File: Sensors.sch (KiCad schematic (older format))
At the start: 0 parts

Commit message: Schematic v0.2
Added IC and wiring
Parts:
- added P11, P13: CONN_01X07, symbol CONN_01X07
- added P12, P14: CONN_01X04, symbol CONN_01X04
- added P15: DHT22, symbol CONN_01X03
- added P16: GY-87, symbol CONN_01X08
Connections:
- new net +BATT: P11.2 (P2), P13.1 (P1), P15.2 (P2), P16.1 (P1)
- new net A0: P12.4 (P4)
- new net A1: P12.3 (P3)
- new net A2: P12.2 (P2)
- new net A3: P12.1 (P1)
- new net D7: P14.3 (P3)
- new net D8: P14.4 (P4)
- new net DHT/D6: P11.7 (P7), P15.1 (P1)
- new net DRDY: P16.8 (P8)
- new net FSYNC: P16.6 (P6)
- new net GND: P11.1 (P1), P13.2 (P2), P15.3 (P3), P16.2 (P2)
- new net INT0: P14.1 (P1)
- new net INT1: P14.2 (P2)
- new net INTA: P16.7 (P7)
- new net MISO: P13.4 (P4)
- new net MOSI: P13.5 (P5)
- new net NSS: P13.6 (P6)
- new net RST: P13.7 (P7)
- new net SCK: P13.3 (P3)
- new net SCL: P11.3 (P3), P16.4 (P4)
- new net SDA: P11.4 (P4), P16.5 (P5)
- new net S_RX: P11.5 (P5)
- new net S_TX: P11.6 (P6)
- no-connect marks 0 -> 4

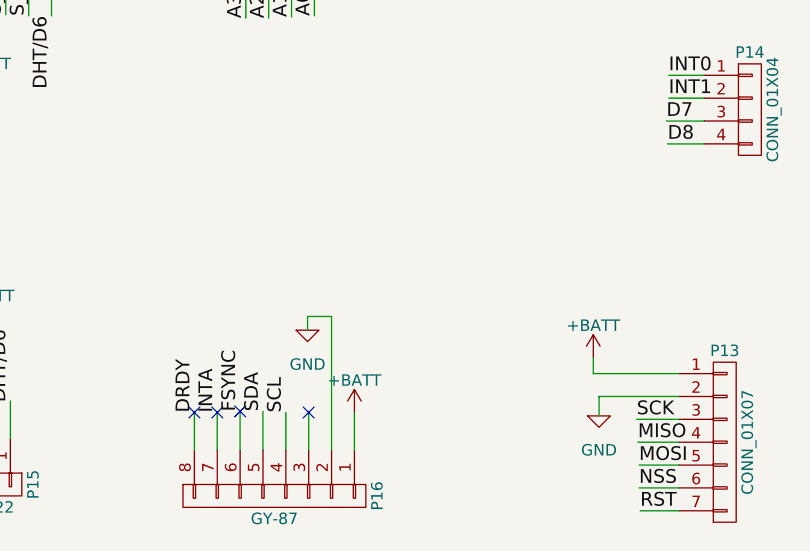
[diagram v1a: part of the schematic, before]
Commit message: Fix arduino mini pro pin 6 bug, added capacitors
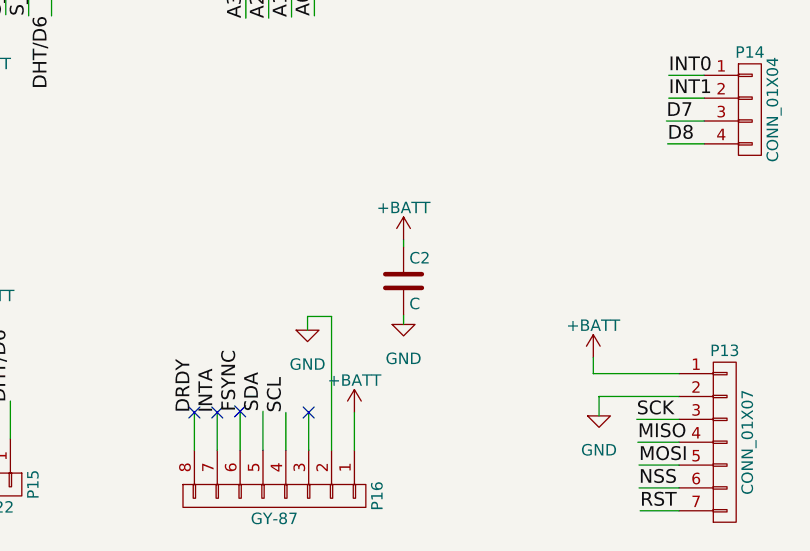
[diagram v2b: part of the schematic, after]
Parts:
- added C2: C, symbol C
- P11, P13: footprint (none) -> Pin_Headers:Pin_Header_Straight_1x07
- P12, P14: footprint (none) -> Pin_Headers:Pin_Header_Straight_1x04
- P15: footprint (none) -> Pin_Headers:Pin_Header_Straight_1x03
- P16: footprint (none) -> Pin_Headers:Pin_Header_Straight_1x08
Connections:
- net +BATT: now also C2.1
- net GND: now also C2.2
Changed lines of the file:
@@
 EESchema Schematic File Version 2
+LIBS:CatSat-rescue
 LIBS:power
 LIBS:device
@@
 LIBS:contrib
 LIBS:valves
-LIBS:ArduProMiniTKB
-LIBS:L80-M39
-LIBS:RFM95W-868S2
-LIBS:theinventorhouse
 LIBS:CatSat-cache
+LIBS:rfm95
 EELAYER 25 0
 EELAYER END
@@
 F 0 "P13" H 7765 5020 50  0000 C CNN
 F 1 "CONN_01X07" V 7865 4620 50  0000 C CNN
-F 2 "" H 7765 4620 50  0000 C CNN
+F 2 "Pin_Headers:Pin_Header_Straight_1x07" H 7765 4620 50  0001 C CNN
 F 3 "" H 7765 4620 50  0000 C CNN
 	1    7765 4620
@@
 F 0 "P14" H 7875 3415 50  0000 C CNN
 F 1 "CONN_01X04" V 7975 3165 50  0000 C CNN
-F 2 "" H 7875 3165 50  0000 C CNN
+F 2 "Pin_Headers:Pin_Header_Straight_1x04" H 7875 3165 50  0001 C CNN
 F 3 "" H 7875 3165 50  0000 C CNN
 	1    7875 3165
@@
 F 0 "P12" H 5820 2625 50  0000 C CNN
 F 1 "CONN_01X04" V 5920 2375 50  0000 C CNN
-F 2 "" H 5820 2375 50  0000 C CNN
+F 2 "Pin_Headers:Pin_Header_Straight_1x04" H 5820 2375 50  0001 C CNN
 F 3 "" H 5820 2375 50  0000 C CNN
 	1    5820 2375
@@
 F 0 "P11" H 4520 2780 50  0000 C CNN
 F 1 "CONN_01X07" V 4620 2380 50  0000 C CNN
-F 2 "" H 4520 2380 50  0000 C CNN
+F 2 "Pin_Headers:Pin_Header_Straight_1x07" H 4520 2380 50  0001 C CNN
 F 3 "" H 4520 2380 50  0000 C CNN
 	1    4520 2380
@@
 $EndComp
 $Comp
-L +BATT #PWR017
+L +BATT #PWR021
 U 1 1 579A5A93
 P 4525 3105
-F 0 "#PWR017" H 4525 2955 50  0001 C CNN
+F 0 "#PWR021" H 4525 2955 50  0001 C CNN
 F 1 "+BATT" H 4525 3245 50  0000 C CNN
 F 2 "" H 4525 3105 50  0000 C CNN
@@
 A0
 $Comp
-L GND #PWR018
+L GND #PWR022
 U 1 1 579A5AA2
 P 4220 2650
-F 0 "#PWR018" H 4220 2400 50  0001 C CNN
+F 0 "#PWR022" H 4220 2400 50  0001 C CNN
 F 1 "GND" H 4220 2500 50  0000 C CNN
 F 2 "" H 4220 2650 50  0000 C CNN
@@
 A3
 $Comp
-L GND #PWR019
+L GND #PWR023
 U 1 1 579A7C37
 P 7215 4505
-F 0 "#PWR019" H 7215 4255 50  0001 C CNN
+F 0 "#PWR023" H 7215 4255 50  0001 C CNN
 F 1 "GND" H 7215 4355 50  0000 C CNN
 F 2 "" H 7215 4505 50  0000 C CNN
@@
 $EndComp
 $Comp
-L +BATT #PWR020
+L +BATT #PWR024
 U 1 1 579A7C57
 P 7190 4250
-F 0 "#PWR020" H 7190 4100 50  0001 C CNN
+F 0 "#PWR024" H 7190 4100 50  0001 C CNN
 F 1 "+BATT" H 7190 4390 50  0000 C CNN
 F 2 "" H 7190 4250 50  0000 C CNN
@@
 F 0 "P15" H 4540 5005 50  0000 C CNN
 F 1 "DHT22" V 4640 4805 50  0000 C CNN
-F 2 "" H 4540 4805 50  0000 C CNN
+F 2 "Pin_Headers:Pin_Header_Straight_1x03" H 4540 4805 50  0001 C CNN
 F 3 "" H 4540 4805 50  0000 C CNN
 	1    4540 4805
@@
 F 0 "P16" H 5795 5305 50  0000 C CNN
 F 1 "GY-87" V 5895 4855 50  0000 C CNN
-F 2 "" H 5795 4855 50  0000 C CNN
+F 2 "Pin_Headers:Pin_Header_Straight_1x08" H 5795 4855 50  0001 C CNN
 F 3 "" H 5795 4855 50  0000 C CNN
 	1    5795 4855
@@
 SCL
 $Comp
-L +BATT #PWR021
+L +BATT #PWR025
 U 1 1 579A9426
 P 6145 4490
-F 0 "#PWR021" H 6145 4340 50  0001 C CNN
+F 0 "#PWR025" H 6145 4340 50  0001 C CNN
 F 1 "+BATT" H 6145 4630 50  0000 C CNN
 F 2 "" H 6145 4490 50  0000 C CNN
@@
 $EndComp
 $Comp
-L GND #PWR022
+L GND #PWR026
 U 1 1 579A9468
 P 5940 4130
-F 0 "#PWR022" H 5940 3880 50  0001 C CNN
+F 0 "#PWR026" H 5940 3880 50  0001 C CNN
 F 1 "GND" H 5940 3980 50  0000 C CNN
 F 2 "" H 5940 4130 50  0000 C CNN
@@
 NoConn ~ 5945 4490
 $Comp
-L GND #PWR023
+L GND #PWR027
 U 1 1 579A95AE
 P 4280 4450
-F 0 "#PWR023" H 4280 4200 50  0001 C CNN
+F 0 "#PWR027" H 4280 4200 50  0001 C CNN
 F 1 "GND" H 4280 4300 50  0000 C CNN
 F 2 "" H 4280 4450 50  0000 C CNN
@@
 $EndComp
 $Comp
-L +BATT #PWR024
+L +BATT #PWR028
 U 1 1 579A95D4
 P 4540 4120
-F 0 "#PWR024" H 4540 3970 50  0001 C CNN
+F 0 "#PWR028" H 4540 3970 50  0001 C CNN
 F 1 "+BATT" H 4540 4260 50  0000 C CNN
 F 2 "" H 4540 4120 50  0000 C CNN
@@
 NoConn ~ 5545 4490
 NoConn ~ 5645 4485
+$Comp
+L GND #PWR?
+U 1 1 579BCD75
+P 6360 4105
+F 0 "#PWR?" H 6360 3855 50  0001 C CNN
+F 1 "GND" H 6360 3955 50  0000 C CNN
+F 2 "" H 6360 4105 50  0000 C CNN
+F 3 "" H 6360 4105 50  0000 C CNN
+	1    6360 4105
+	1    0    0    -1
+$EndComp
+$Comp
+L +BATT #PWR?
+U 1 1 579BCD92
+P 6360 3735
+F 0 "#PWR?" H 6360 3585 50  0001 C CNN
+F 1 "+BATT" H 6360 3875 50  0000 C CNN
+F 2 "" H 6360 3735 50  0000 C CNN
+F 3 "" H 6360 3735 50  0000 C CNN
+	1    6360 3735
+	1    0    0    -1
+$EndComp
+$Comp
+L C C2
+U 1 1 579BCEC3
+P 6360 3915
+F 0 "C2" H 6385 4015 50  0000 L CNN
+F 1 "C" H 6385 3815 50  0000 L CNN
+F 2 "" H 6398 3765 30  0000 C CNN
+F 3 "" H 6360 3915 60  0000 C CNN
+	1    6360 3915
+	1    0    0    -1
+$EndComp
+Wire Wire Line
+	6360 3765 6360 3735
+Wire Wire Line
+	6360 4065 6360 4105
 $EndSCHEMATC

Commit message: Finished telemtry PCB
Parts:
- C2: footprint (none) -> Capacitors_ThroughHole:C_Disc_D6_P5
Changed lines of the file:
@@
 $EndComp
 $Comp
-L +BATT #PWR021
+L +BATT #PWR025
 U 1 1 579A5A93
 P 4525 3105
-F 0 "#PWR021" H 4525 2955 50  0001 C CNN
+F 0 "#PWR025" H 4525 2955 50  0001 C CNN
 F 1 "+BATT" H 4525 3245 50  0000 C CNN
 F 2 "" H 4525 3105 50  0000 C CNN
@@
 A0
 $Comp
-L GND #PWR022
+L GND #PWR026
 U 1 1 579A5AA2
 P 4220 2650
-F 0 "#PWR022" H 4220 2400 50  0001 C CNN
+F 0 "#PWR026" H 4220 2400 50  0001 C CNN
 F 1 "GND" H 4220 2500 50  0000 C CNN
 F 2 "" H 4220 2650 50  0000 C CNN
@@
 A3
 $Comp
-L GND #PWR023
+L GND #PWR027
 U 1 1 579A7C37
 P 7215 4505
-F 0 "#PWR023" H 7215 4255 50  0001 C CNN
+F 0 "#PWR027" H 7215 4255 50  0001 C CNN
 F 1 "GND" H 7215 4355 50  0000 C CNN
 F 2 "" H 7215 4505 50  0000 C CNN
@@
 $EndComp
 $Comp
-L +BATT #PWR024
+L +BATT #PWR028
 U 1 1 579A7C57
 P 7190 4250
-F 0 "#PWR024" H 7190 4100 50  0001 C CNN
+F 0 "#PWR028" H 7190 4100 50  0001 C CNN
 F 1 "+BATT" H 7190 4390 50  0000 C CNN
 F 2 "" H 7190 4250 50  0000 C CNN
@@
 SCL
 $Comp
-L +BATT #PWR025
+L +BATT #PWR029
 U 1 1 579A9426
 P 6145 4490
-F 0 "#PWR025" H 6145 4340 50  0001 C CNN
+F 0 "#PWR029" H 6145 4340 50  0001 C CNN
 F 1 "+BATT" H 6145 4630 50  0000 C CNN
 F 2 "" H 6145 4490 50  0000 C CNN
@@
 $EndComp
 $Comp
-L GND #PWR026
+L GND #PWR030
 U 1 1 579A9468
 P 5940 4130
-F 0 "#PWR026" H 5940 3880 50  0001 C CNN
+F 0 "#PWR030" H 5940 3880 50  0001 C CNN
 F 1 "GND" H 5940 3980 50  0000 C CNN
 F 2 "" H 5940 4130 50  0000 C CNN
@@
 NoConn ~ 5945 4490
 $Comp
-L GND #PWR027
+L GND #PWR031
 U 1 1 579A95AE
 P 4280 4450
-F 0 "#PWR027" H 4280 4200 50  0001 C CNN
+F 0 "#PWR031" H 4280 4200 50  0001 C CNN
 F 1 "GND" H 4280 4300 50  0000 C CNN
 F 2 "" H 4280 4450 50  0000 C CNN
@@
 $EndComp
 $Comp
-L +BATT #PWR028
+L +BATT #PWR032
 U 1 1 579A95D4
 P 4540 4120
-F 0 "#PWR028" H 4540 3970 50  0001 C CNN
+F 0 "#PWR032" H 4540 3970 50  0001 C CNN
 F 1 "+BATT" H 4540 4260 50  0000 C CNN
 F 2 "" H 4540 4120 50  0000 C CNN
@@
 NoConn ~ 5645 4485
 $Comp
-L GND #PWR?
+L GND #PWR033
 U 1 1 579BCD75
 P 6360 4105
-F 0 "#PWR?" H 6360 3855 50  0001 C CNN
+F 0 "#PWR033" H 6360 3855 50  0001 C CNN
 F 1 "GND" H 6360 3955 50  0000 C CNN
 F 2 "" H 6360 4105 50  0000 C CNN
@@
 $EndComp
 $Comp
-L +BATT #PWR?
+L +BATT #PWR034
 U 1 1 579BCD92
 P 6360 3735
-F 0 "#PWR?" H 6360 3585 50  0001 C CNN
+F 0 "#PWR034" H 6360 3585 50  0001 C CNN
 F 1 "+BATT" H 6360 3875 50  0000 C CNN
 F 2 "" H 6360 3735 50  0000 C CNN
@@
 F 0 "C2" H 6385 4015 50  0000 L CNN
 F 1 "C" H 6385 3815 50  0000 L CNN
-F 2 "" H 6398 3765 30  0000 C CNN
+F 2 "Capacitors_ThroughHole:C_Disc_D6_P5" H 6398 3765 30  0001 C CNN
 F 3 "" H 6360 3915 60  0000 C CNN
 	1    6360 3915

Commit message: PCB final
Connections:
- net GND: now also P16.3 (P3); no longer P16.2 (P2)
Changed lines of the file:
@@
 $EndComp
 $Comp
-L +BATT #PWR025
+L +BATT #PWR027
 U 1 1 579A5A93
 P 4525 3105
-F 0 "#PWR025" H 4525 2955 50  0001 C CNN
+F 0 "#PWR027" H 4525 2955 50  0001 C CNN
 F 1 "+BATT" H 4525 3245 50  0000 C CNN
 F 2 "" H 4525 3105 50  0000 C CNN
@@
 A0
 $Comp
-L GND #PWR026
+L GND #PWR028
 U 1 1 579A5AA2
 P 4220 2650
-F 0 "#PWR026" H 4220 2400 50  0001 C CNN
+F 0 "#PWR028" H 4220 2400 50  0001 C CNN
 F 1 "GND" H 4220 2500 50  0000 C CNN
 F 2 "" H 4220 2650 50  0000 C CNN
@@
 A3
 $Comp
-L GND #PWR027
+L GND #PWR029
 U 1 1 579A7C37
 P 7215 4505
-F 0 "#PWR027" H 7215 4255 50  0001 C CNN
+F 0 "#PWR029" H 7215 4255 50  0001 C CNN
 F 1 "GND" H 7215 4355 50  0000 C CNN
 F 2 "" H 7215 4505 50  0000 C CNN
@@
 $EndComp
 $Comp
-L +BATT #PWR028
+L +BATT #PWR030
 U 1 1 579A7C57
 P 7190 4250
-F 0 "#PWR028" H 7190 4100 50  0001 C CNN
+F 0 "#PWR030" H 7190 4100 50  0001 C CNN
 F 1 "+BATT" H 7190 4390 50  0000 C CNN
 F 2 "" H 7190 4250 50  0000 C CNN
@@
 	5845 4655 5845 4490
 Wire Wire Line
-	5945 4655 5945 4490
-Wire Wire Line
-	6045 4070 6045 4655
+	5945 4400 5945 4655
 Wire Wire Line
 	6145 4655 6145 4490
@@
 SCL
 $Comp
-L +BATT #PWR029
+L +BATT #PWR031
 U 1 1 579A9426
 P 6145 4490
-F 0 "#PWR029" H 6145 4340 50  0001 C CNN
+F 0 "#PWR031" H 6145 4340 50  0001 C CNN
 F 1 "+BATT" H 6145 4630 50  0000 C CNN
 F 2 "" H 6145 4490 50  0000 C CNN
@@
 $EndComp
 $Comp
-L GND #PWR030
+L GND #PWR032
 U 1 1 579A9468
 P 5940 4130
-F 0 "#PWR030" H 5940 3880 50  0001 C CNN
+F 0 "#PWR032" H 5940 3880 50  0001 C CNN
 F 1 "GND" H 5940 3980 50  0000 C CNN
 F 2 "" H 5940 4130 50  0000 C CNN
@@
 Wire Wire Line
 	5940 4070 6045 4070
-NoConn ~ 5945 4490
-$Comp
-L GND #PWR031
+$Comp
+L GND #PWR033
 U 1 1 579A95AE
 P 4280 4450
-F 0 "#PWR031" H 4280 4200 50  0001 C CNN
+F 0 "#PWR033" H 4280 4200 50  0001 C CNN
 F 1 "GND" H 4280 4300 50  0000 C CNN
 F 2 "" H 4280 4450 50  0000 C CNN
@@
 $EndComp
 $Comp
-L +BATT #PWR032
+L +BATT #PWR034
 U 1 1 579A95D4
 P 4540 4120
-F 0 "#PWR032" H 4540 3970 50  0001 C CNN
+F 0 "#PWR034" H 4540 3970 50  0001 C CNN
 F 1 "+BATT" H 4540 4260 50  0000 C CNN
 F 2 "" H 4540 4120 50  0000 C CNN
@@
 NoConn ~ 5645 4485
 $Comp
-L GND #PWR033
+L GND #PWR035
 U 1 1 579BCD75
 P 6360 4105
-F 0 "#PWR033" H 6360 3855 50  0001 C CNN
+F 0 "#PWR035" H 6360 3855 50  0001 C CNN
 F 1 "GND" H 6360 3955 50  0000 C CNN
 F 2 "" H 6360 4105 50  0000 C CNN
@@
 $EndComp
 $Comp
-L +BATT #PWR034
+L +BATT #PWR036
 U 1 1 579BCD92
 P 6360 3735
-F 0 "#PWR034" H 6360 3585 50  0001 C CNN
+F 0 "#PWR036" H 6360 3585 50  0001 C CNN
 F 1 "+BATT" H 6360 3875 50  0000 C CNN
 F 2 "" H 6360 3735 50  0000 C CNN
@@
 Wire Wire Line
 	6360 4065 6360 4105
+Wire Wire Line
+	6045 4070 6045 4400
+Wire Wire Line
+	6045 4400 5945 4400
+Wire Wire Line
+	6045 4655 6045 4495
+NoConn ~ 6045 4495
 $EndSCHEMATC
